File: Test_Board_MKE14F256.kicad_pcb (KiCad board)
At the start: 4 copper layers, 62.8 x 49.7 mm, 115 parts, among them P1 CONN_01X02, P2 CONN_01X04, P28 CONN_01X04, P3 CONN_01X02, P4 CONN_01X04, P5 CONN_01X05, P6 CONN_01X04, U1 TS30042, U2 NCP700B, U3 MIC2288, U4 ADS79XX, U5 REF3030, U6 TSV524A, U7 MKE14F256_v.1.2, Y1 ABMM2-8.000MHZ-E2-T

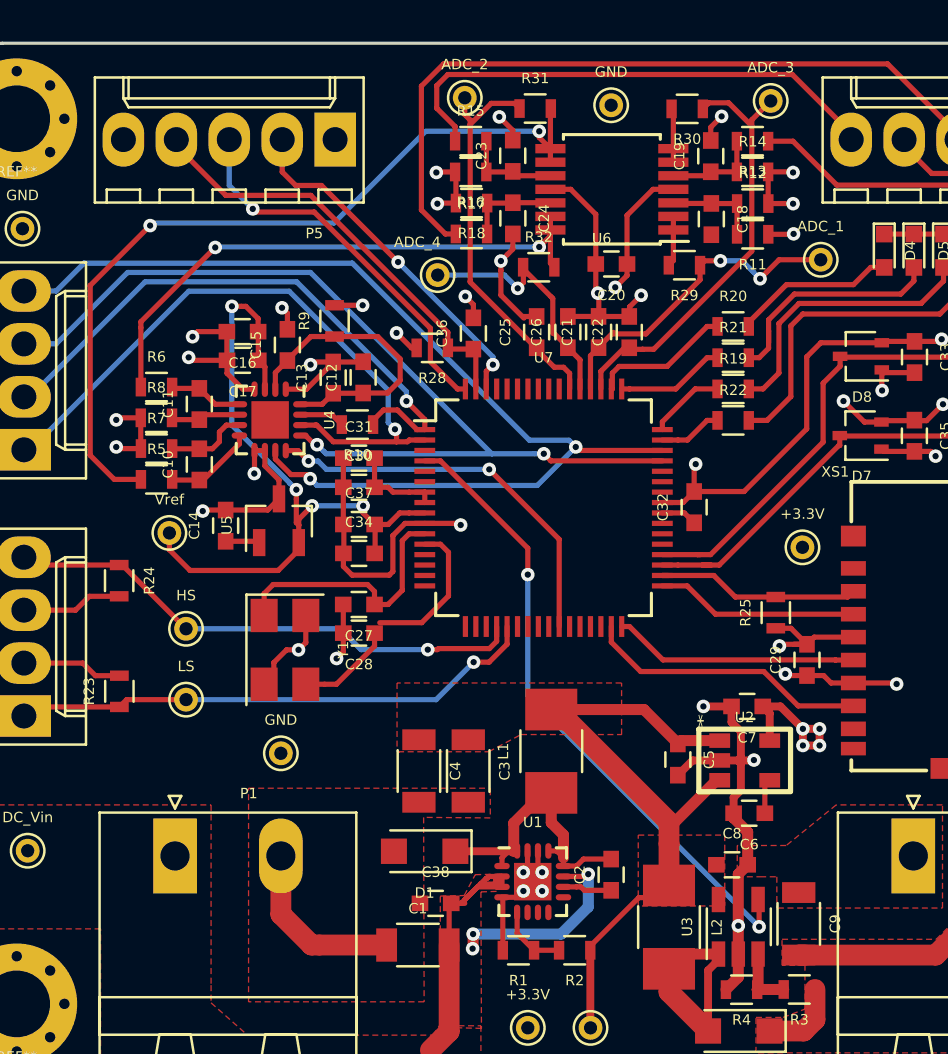
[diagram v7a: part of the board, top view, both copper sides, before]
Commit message: Fixed some DRC errors
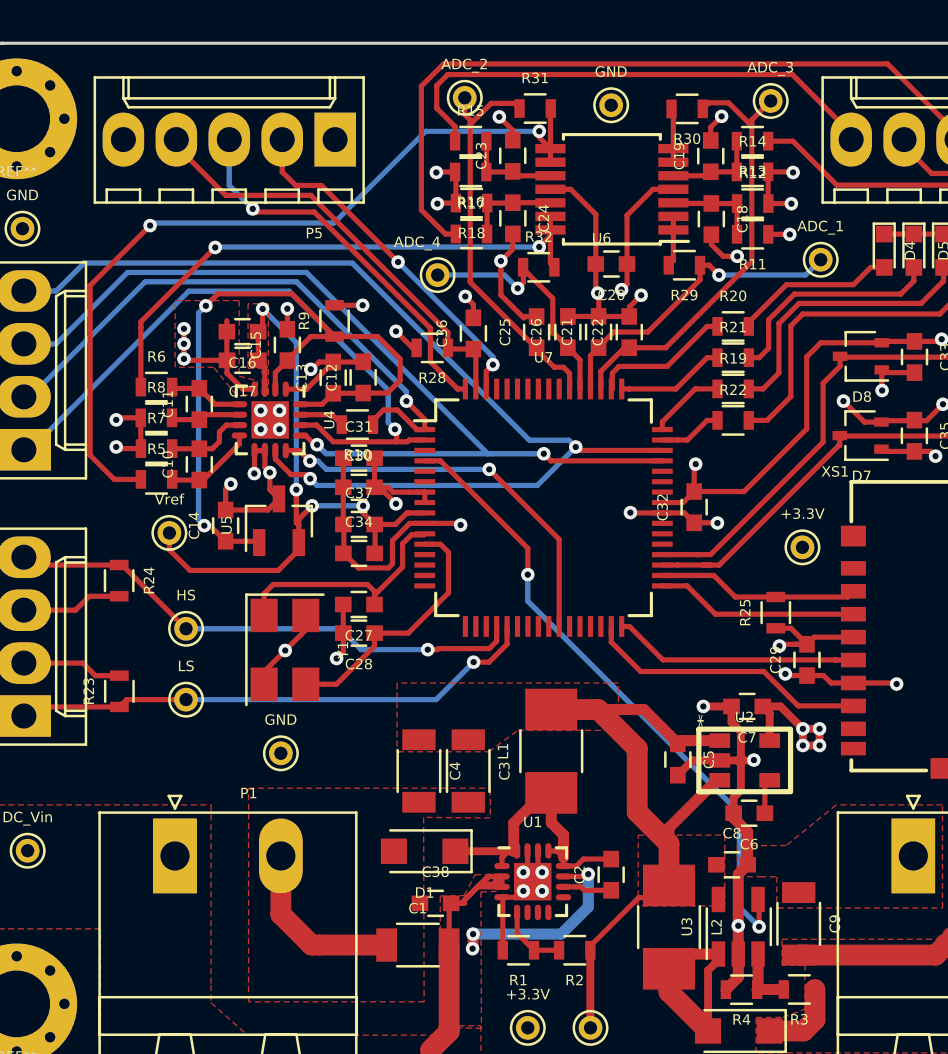
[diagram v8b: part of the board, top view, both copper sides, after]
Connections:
- Y1 pad 2: (no net) -> GND
- Y1 pad 4: (no net) -> GND
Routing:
- net Net-(C12-Pad1): track 15.9 -> 35.5 mm, vias 0 -> 2
- net GND: track 149.2 -> 161.3 mm, vias 35 -> 45
- net (no net): track 4.46 -> 0.00 mm, vias 1 -> 0
- net DC_3V6: track 33.1 -> 35.4 mm
- net Vref: track 34.9 -> 33.2 mm
- net +3V3: track 53.9 -> 55.1 mm, vias 13 -> 14
- net ADC_1: track 15.7 -> 15.4 mm, vias 2 -> 1
- added copper zone on +3.3V, net +3V3
- added copper zone on GND, net GND
- added copper zone on F.Cu, net Vref
